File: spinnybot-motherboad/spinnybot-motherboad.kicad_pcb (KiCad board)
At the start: 2 copper layers, 109.4 x 86 mm, 86 parts, among them J1 ENCODER 1, J10 ESC_POS, J11 POWER SW2, J12 LEDSTRIP3, J13 LEDSTRIP2, J14 LEDSTRIP3, J15 BAT_GND, J16 ESC_GND, J2 LEDSTRIP1, J3 LEDSTRIP1, J4 LEDSTRIP2, J5 ENCODER 2, J6 ENCODER 3, J7 SM10B-SRSS-TB, J8 BAT_POS, J9 POWER SW1, Q1 SISA96DN, Q2 SISA96DN, Q3 BC846, Q4 BC846, U1 LM1117-3.3, U10 MMA3221KEG, U11 ADS122U04IPWR, U12 ADS122U04IPWR, U2 XBP9B-DMWTB002, U3 MC14504BDR2G, U4 ICM-20649, U5 ESP32-DEVKITC-32D, U6 74LVC1G157GV_125, U7 SN74AHCT541DW, U8 SN74LVC1G18DBVR, U9 MMA3221KEG

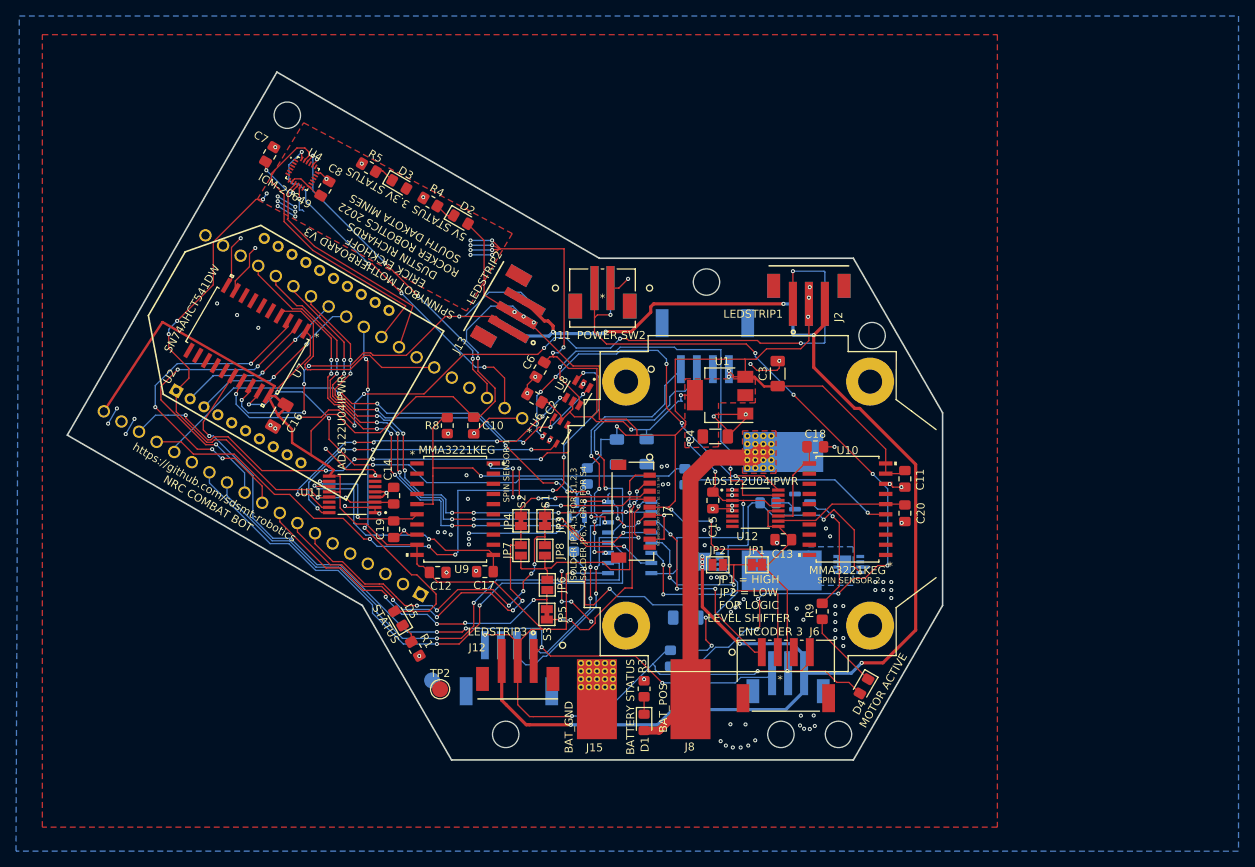
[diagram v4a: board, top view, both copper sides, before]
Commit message: adjust mounting holes to have pads and change locations
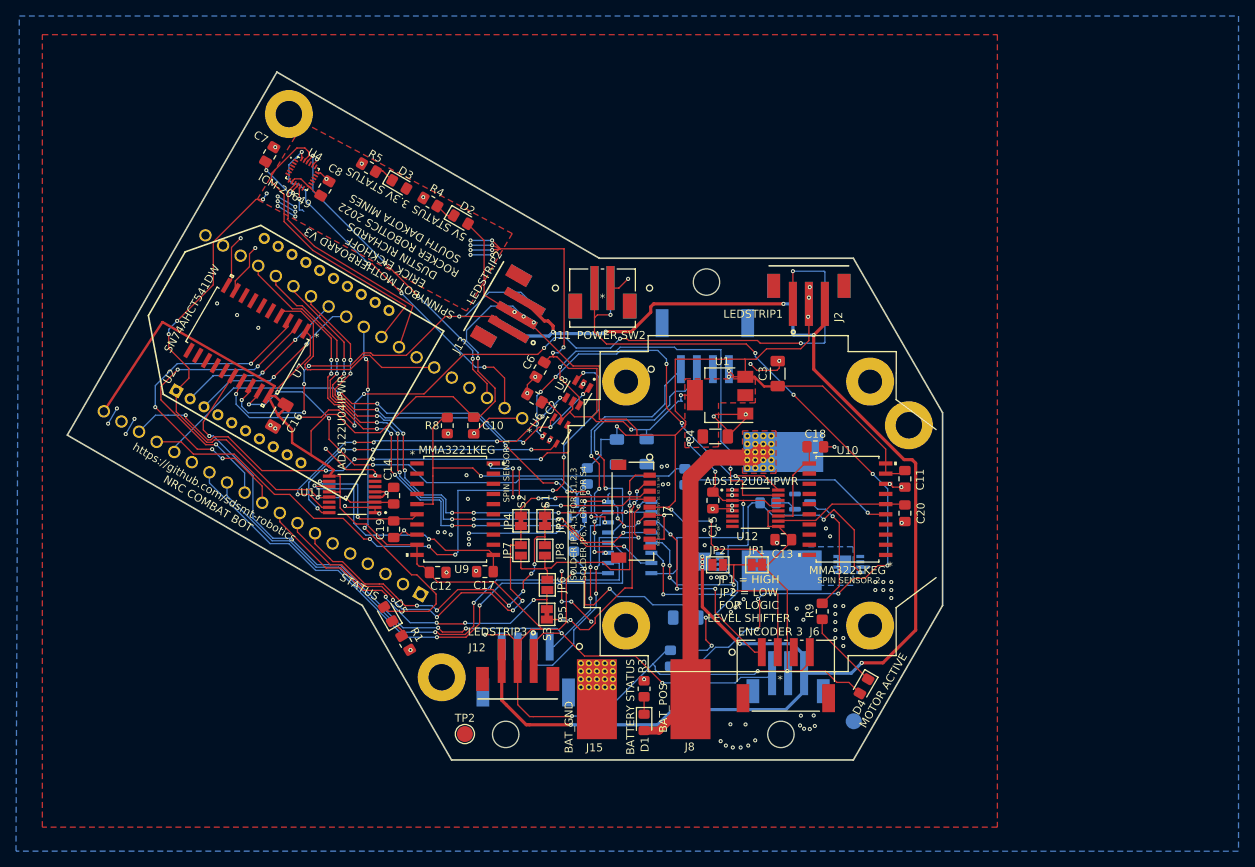
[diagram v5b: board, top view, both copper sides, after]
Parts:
- H2, H5, H6: footprint custom:MountingHole_3.3mm -> custom:StrainHole_3.3mm
- moved H4 68.7 mm to (134.9, 139.8)
- moved TP1 52.9 mm to (186.4, 145.3)
- moved H1 39.6 mm to (193.3, 108.3)
- moved TP2 6.40 mm to (137.8, 146.9)
- moved J5 2.11 mm to (145.4, 138.9)
- moved R1 1.41 mm to (130.4, 135.5)
- moved D5 1.41 mm to (128.2, 131.9)
- moved H3 0.25 mm to (115.8, 69.4)
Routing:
- net /LEDSTRIP3_DATA_5V: track 99.4 -> 102.3 mm
- net /ENC_2A_5V: track 23.8 -> 21.1 mm
- net Net-(D5-Pad2): track 44.7 -> 46.2 mm
- net /MCU and Buffers/ENC_1B_3V3: track 72.5 -> 71.2 mm
- net /MCU and Buffers/ENC_1A_3V3: track 66.8 -> 65.9 mm
- net +5V: track 400.8 -> 399.9 mm
- net /ENC_2B_5V: track 34.5 -> 33.9 mm

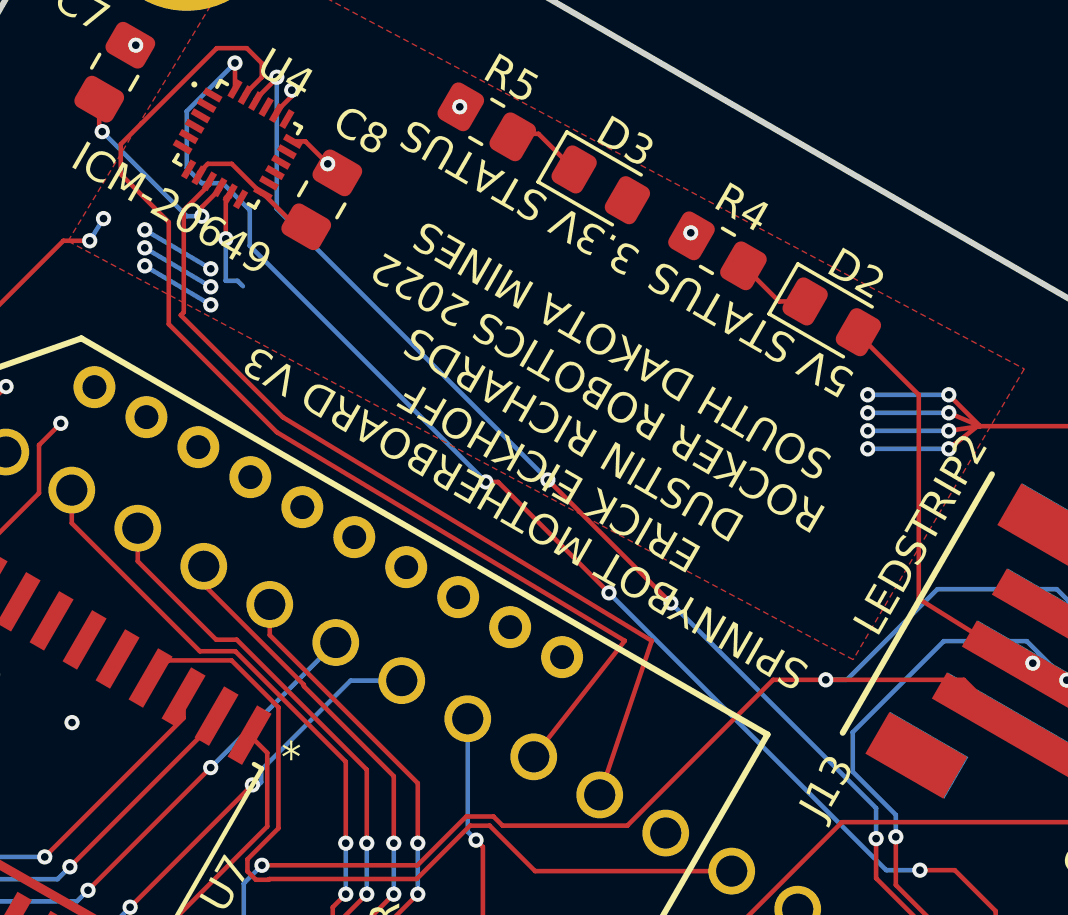
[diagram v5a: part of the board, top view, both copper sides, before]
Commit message: silkscreen fix, add 'THIS BOARD WORKS'
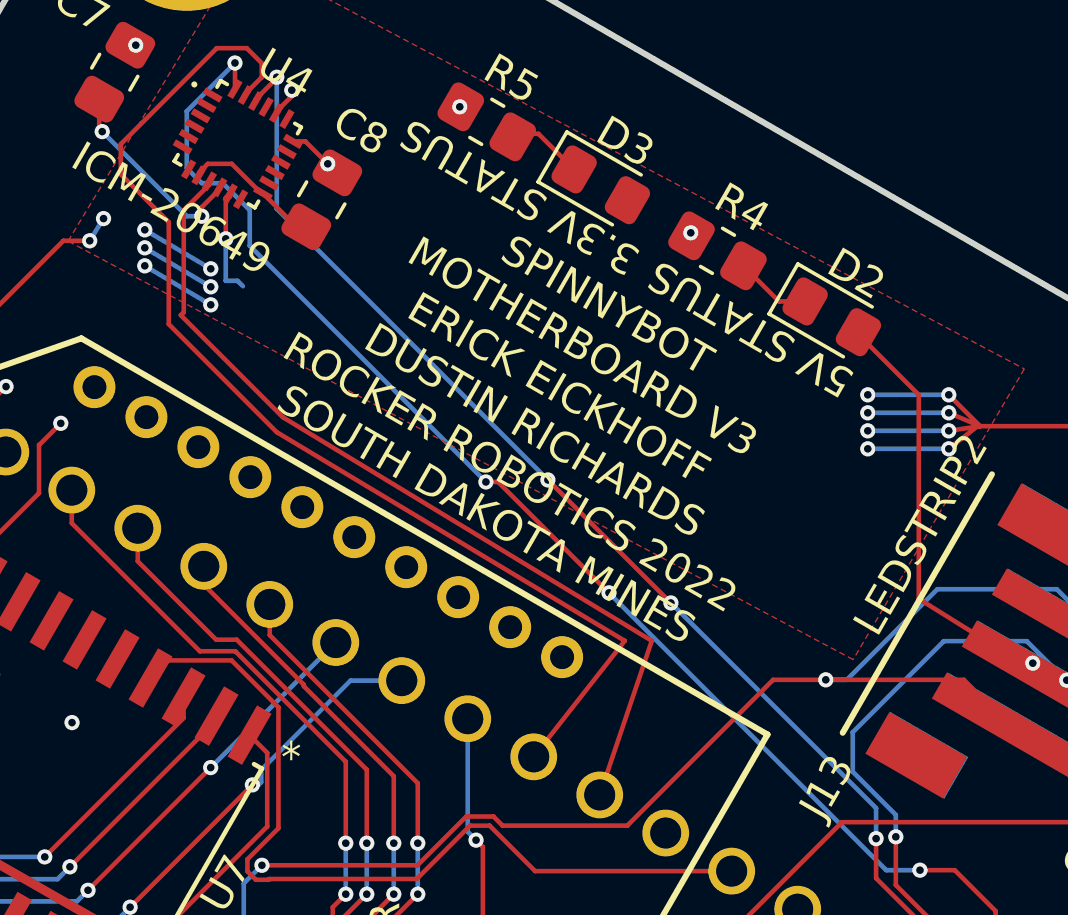
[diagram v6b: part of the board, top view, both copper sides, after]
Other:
- board text added: "THIS BOARD WORKS"
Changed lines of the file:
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@@
+    (effects (font (size 1 1) (thickness 0.15)) (justify mirror))
+  )
+  (gr_text "THIS BOARD WORKS" (at 129 84.855 150) (layer "B.SilkS")
     (effects (font (size 1 1) (thickness 0.15)) (justify mirror))
   )
@@
     (effects (font (size 1 1) (thickness 0.15)))
   )
-  (gr_text "SPINNYBOT MOTHERBOARD V3\nERICK EICKHOFF\nDUSTIN RICHARDS\nROCKER ROBOTICS 2022\nSOUTH DAKOTA MINES" (at 128.7 86.455 150) (layer "F.SilkS")
-    (effects (font (size 1 1) (thickness 0.15)))
-  )
   (gr_text "SPIN SENSOR 1" (at 143 113.955 90) (layer "F.SilkS")
     (effects (font (size 0.75 0.75) (thickness 0.15)))
   )
+  (gr_text "SPINNYBOT\nMOTHERBOARD V3\nERICK EICKHOFF\nDUSTIN RICHARDS\nROCKER ROBOTICS 2022\nSOUTH DAKOTA MINES" (at 127.8 85.655 330) (layer "F.SilkS")
+    (effects (font (size 1 1) (thickness 0.15)))
+  )
   (gr_text "N/C GND BAT CRT GND 5V  S1  S2  S3  S4\n" (at 162 119.055 90) (layer "F.SilkS")
